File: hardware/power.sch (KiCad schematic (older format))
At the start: 34 parts, among them Q1 2n7002w, Q2 mmbt3906wt1, Q3 si2327ds, U1 TPS54526_PWP, U2 LT1761_1, U3 MIC2774N

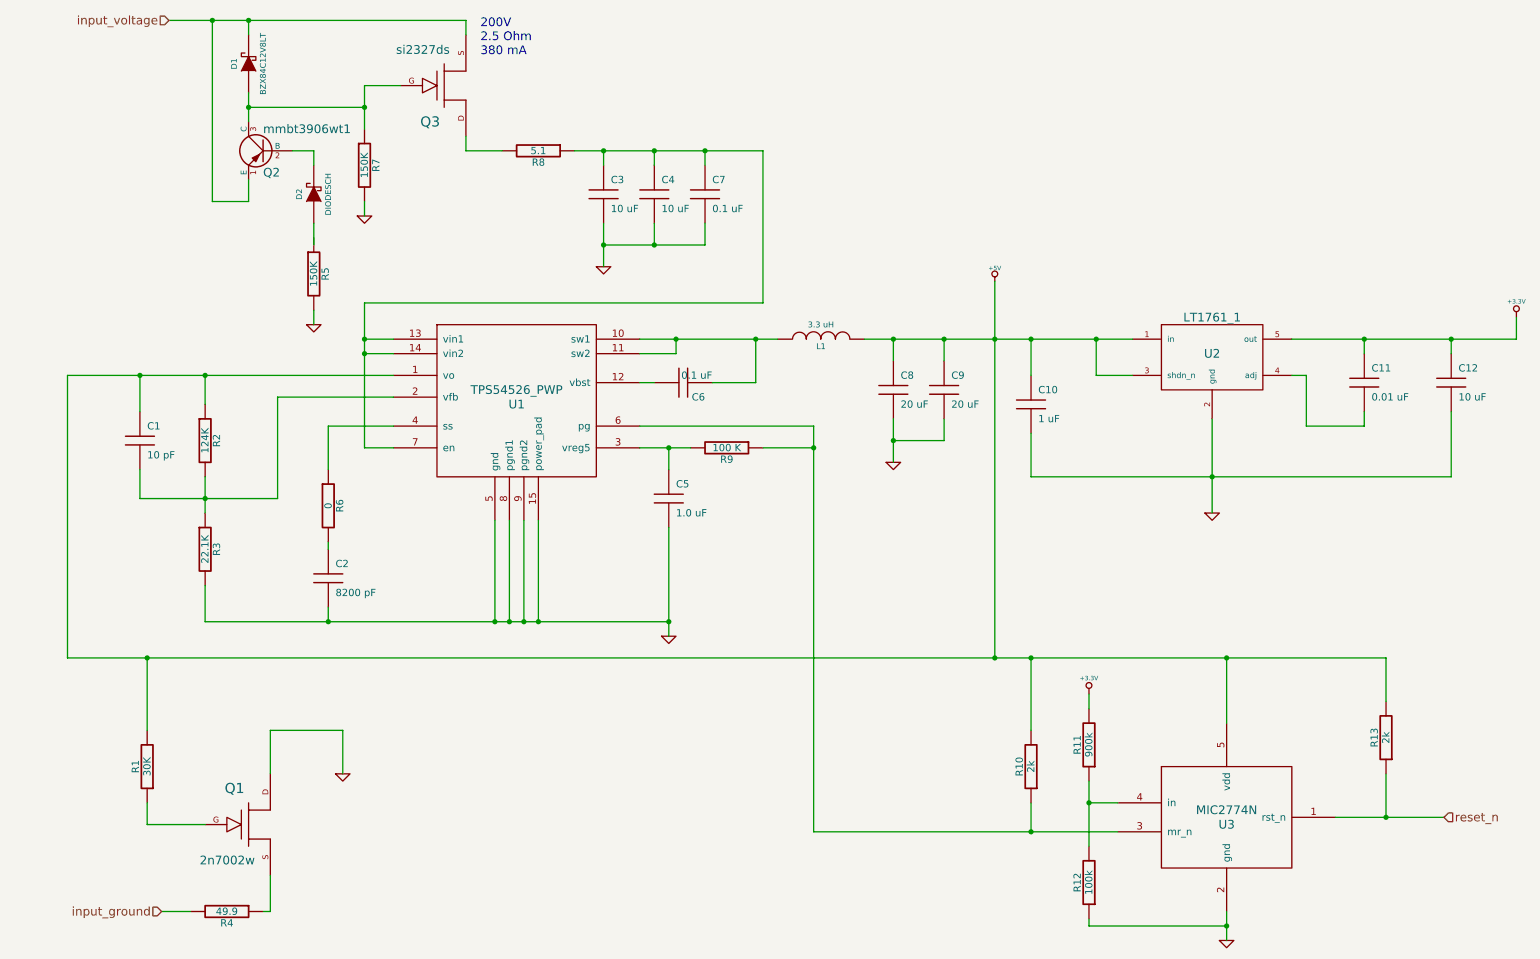
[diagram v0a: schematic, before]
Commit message: removed some protection
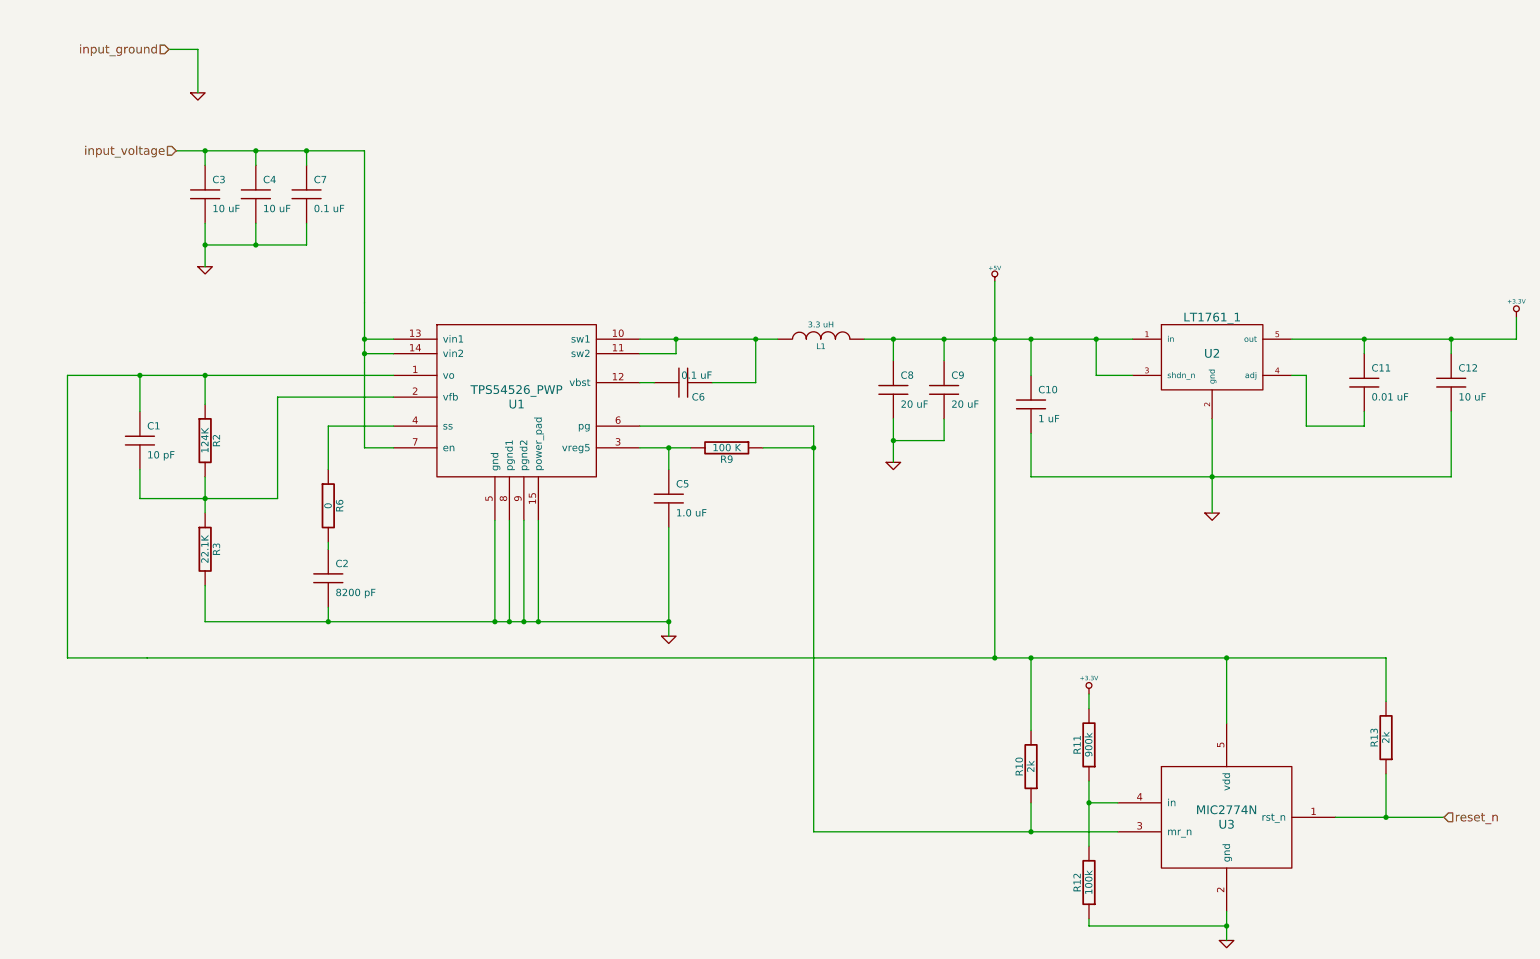
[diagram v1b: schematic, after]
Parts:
- removed D1: BZX84C12V8LT, symbol DIODESCH
- removed D2: DIODESCH, symbol DIODESCH
- removed Q1: 2n7002w, symbol FET_N
- removed Q2: mmbt3906wt1, symbol PNP
- removed Q3: si2327ds, symbol FET_N
- removed R1: 30K, symbol R
- removed R4: 49.9, symbol R
- removed R5, R7: 150K, symbol R
- removed R8: 5.1, symbol R
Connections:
- net input_voltage: now also C3.1, C4.1, C7.1, U1.13 (vin1), U1.14 (vin2), U1.7 (en)
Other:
- note removed: "200V \n2.5 Ohm \n380 mA"
- moved on the sheet: C3, C4, C7

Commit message: updated schematics to include new library and added uSD drive to processor
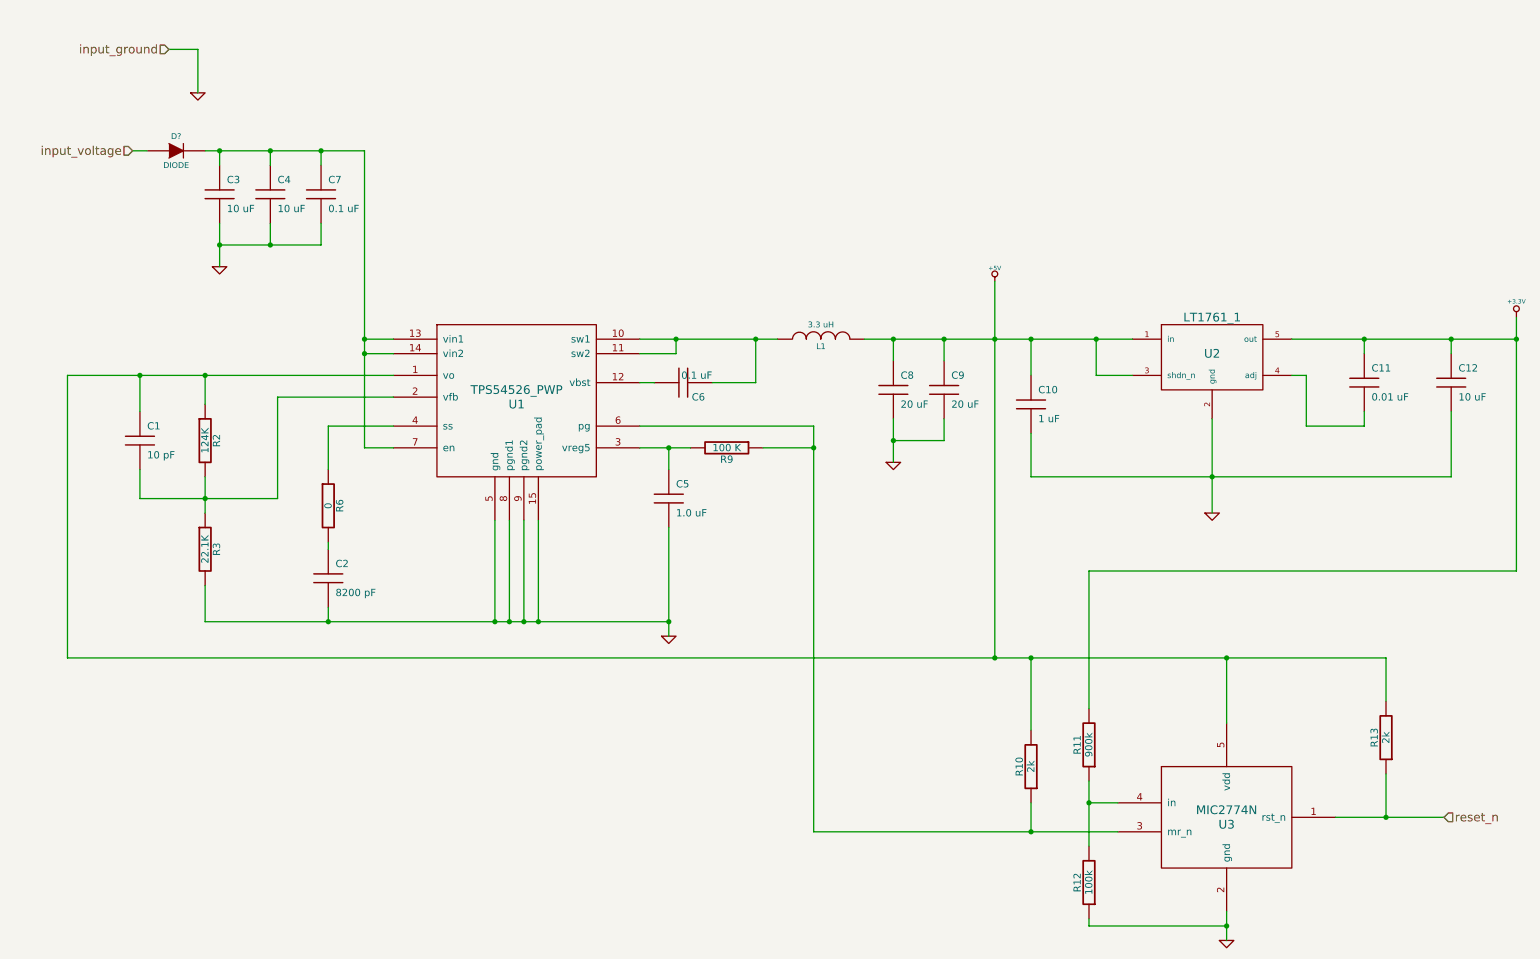
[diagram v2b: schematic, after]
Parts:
- added D?: DIODE, symbol DIODE
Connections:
- net input_voltage: now also D?.1 (A); no longer C3.1, C4.1, C7.1, U1.13 (vin1), U1.14 (vin2), U1.7 (en)
- new net: C3.1, C4.1, C7.1, D?.2 (K), U1.13 (vin1), U1.14 (vin2), U1.7 (en)
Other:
- moved on the sheet: C3, C4, C7
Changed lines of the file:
@@
-EESchema Schematic File Version 2  date Tue 04 Mar 2014 01:13:50 PM EST
+EESchema Schematic File Version 2  date Sat 26 Apr 2014 10:24:32 PM EDT
 LIBS:power
 LIBS:device
@@
 LIBS:valves
 LIBS:gs
+LIBS:opendous
 LIBS:eng_mon-cache
 EELAYER 25  0
@@
 Sheet 3 6
 Title ""
-Date "4 mar 2014"
+Date "27 apr 2014"
 Rev ""
 Comp ""
@@
 Comment4 ""
 $EndDescr
-Wire Wire Line
-	850  5100 1400 5100
-Wire Wire Line
-	1400 5100 7250 5100
+Connection ~ 10850 2900
+Wire Wire Line
+	10850 2750 10850 4500
+Wire Wire Line
+	10850 4500 7900 4500
+Wire Wire Line
+	7900 4500 7900 5450
+Wire Wire Line
+	1300 1600 1400 1600
 Connection ~ 5000 4850
 Wire Wire Line
-	5000 4950 5000 4850
-Wire Wire Line
-	5000 4850 5000 4200
-Wire Wire Line
-	2900 2650 2900 1600
-Wire Wire Line
-	2900 2650 2900 2650
-Wire Wire Line
-	2900 2650 2900 2900
-Wire Wire Line
-	2900 2900 2900 3000
-Wire Wire Line
-	2900 3000 2900 3650
+	5000 4200 5000 4950
+Wire Wire Line
+	2900 3650 2900 1600
 Wire Wire Line
 	1550 900  1750 900
 Wire Wire Line
-	7250 5100 7250 2900
-Wire Wire Line
-	7250 2900 7250 2500
-Wire Wire Line
-	8200 2900 7950 2900
-Wire Wire Line
-	7950 2900 7500 2900
-Wire Wire Line
-	7500 2900 7250 2900
-Wire Wire Line
-	7250 2900 6900 2900
-Wire Wire Line
-	6900 2900 6550 2900
-Wire Wire Line
-	6550 2900 6350 2900
+	7250 2500 7250 5100
+Wire Wire Line
+	6350 2900 8200 2900
 Connection ~ 6000 3650
 Connection ~ 7500 6300
 Wire Wire Line
-	8100 6300 7500 6300
-Wire Wire Line
-	7500 6300 6000 6300
-Wire Wire Line
-	6000 6300 6000 3650
-Wire Wire Line
-	6000 3650 6000 3500
+	8100 6300 6000 6300
+Wire Wire Line
+	6000 6300 6000 3500
 Connection ~ 4100 4850
 Wire Wire Line
-	5150 3650 5000 3650
-Wire Wire Line
-	5000 3650 4800 3650
+	4800 3650 5150 3650
 Connection ~ 1350 3150
 Wire Wire Line
@@
 	4800 3200 4900 3200
 Wire Wire Line
-	4800 2900 5050 2900
-Wire Wire Line
-	5050 2900 5600 2900
-Wire Wire Line
-	5600 2900 5750 2900
+	5750 2900 4800 2900
 Connection ~ 3900 4850
 Wire Wire Line
@@
 Wire Wire Line
 	3800 4850 3800 4150
-Connection ~ 1800 2250
-Wire Wire Line
-	1800 2250 2150 2250
-Wire Wire Line
-	2150 2250 2500 2250
-Wire Wire Line
-	2500 2250 2500 2100
-Connection ~ 2500 1600
-Wire Wire Line
-	2500 1700 2500 1600
-Wire Wire Line
-	1800 1600 1800 1700
+Connection ~ 1900 2250
+Wire Wire Line
+	1900 2250 2600 2250
+Wire Wire Line
+	2600 2250 2600 2100
+Connection ~ 2600 1600
+Wire Wire Line
+	2600 1600 2600 1700
+Wire Wire Line
+	1900 1600 1900 1700
 Wire Wire Line
 	3100 3000 2900 3000
@@
 	7900 6950 7900 6900
 Wire Wire Line
-	7900 5350 7900 5450
-Wire Wire Line
 	7500 6100 7500 6300
 Wire Wire Line
@@
 	9950 5400 9950 5100
 Wire Wire Line
-	9600 6200 9950 6200
-Wire Wire Line
-	9950 6200 10350 6200
+	10350 6200 9600 6200
 Wire Wire Line
 	10400 3400 10400 3850
 Wire Wire Line
-	10400 3850 8750 3850
-Wire Wire Line
-	8750 3850 7500 3850
-Wire Wire Line
-	9300 2900 9800 2900
-Wire Wire Line
-	9800 2900 10400 2900
-Wire Wire Line
-	10400 2900 10850 2900
+	10400 3850 7500 3850
+Wire Wire Line
+	10850 2900 9300 2900
 Connection ~ 9800 2900
 Wire Wire Line
@@
 	7950 3150 8200 3150
 Wire Wire Line
-	8750 4100 8750 3850
-Wire Wire Line
-	8750 3850 8750 3450
+	8750 3450 8750 4100
 Wire Wire Line
 	2650 4300 2650 4350
@@
 Connection ~ 8750 3850
 Wire Wire Line
-	10850 2900 10850 2750
-Wire Wire Line
 	9300 3150 9400 3150
 Wire Wire Line
@@
 Connection ~ 9950 6200
 Wire Wire Line
-	8850 6850 8850 6950
-Wire Wire Line
-	8850 6950 8850 7050
+	8850 7050 8850 6850
 Wire Wire Line
 	7500 5100 7500 5600
 Connection ~ 8850 5100
 Wire Wire Line
-	7900 6400 7900 6100
-Wire Wire Line
-	7900 6100 7900 5950
+	7900 5950 7900 6400
 Connection ~ 7900 6100
 Wire Wire Line
@@
 Connection ~ 2900 2900
 Wire Wire Line
-	2150 1600 2150 1700
-Connection ~ 2150 1600
-Wire Wire Line
-	1800 2100 1800 2250
-Wire Wire Line
-	1800 2250 1800 2400
-Wire Wire Line
-	2150 2100 2150 2250
-Connection ~ 2150 2250
+	2250 1600 2250 1700
+Connection ~ 2250 1600
+Wire Wire Line
+	1900 2400 1900 2100
+Wire Wire Line
+	2250 2100 2250 2250
+Connection ~ 2250 2250
 Wire Wire Line
 	4100 4150 4100 4850
@@
 Connection ~ 5600 2900
 Wire Wire Line
-	6550 3750 6550 3600
-Wire Wire Line
-	6550 3600 6550 3450
+	6550 3450 6550 3750
 Connection ~ 6550 3600
 Wire Wire Line
-	6550 2900 6550 3050
+	6550 3050 6550 2900
 Connection ~ 6550 2900
 Wire Wire Line
@@
 	850  3150 850  5100
 Wire Wire Line
-	850  3150 1350 3150
-Wire Wire Line
-	1350 3150 1800 3150
-Wire Wire Line
-	1800 3150 3100 3150
-Wire Wire Line
-	1800 4850 2650 4850
-Wire Wire Line
-	2650 4850 3800 4850
-Wire Wire Line
-	3800 4850 3900 4850
-Wire Wire Line
-	3900 4850 4000 4850
-Wire Wire Line
-	4000 4850 4100 4850
-Wire Wire Line
-	4100 4850 5000 4850
+	850  3150 3100 3150
+Wire Wire Line
+	1800 4850 5000 4850
 Connection ~ 2650 4850
 Wire Wire Line
-	1800 3850 1800 4000
-Wire Wire Line
-	1800 4000 1800 4100
+	1800 4100 1800 3850
 Wire Wire Line
 	3100 3300 2300 3300
@@
 	1350 3800 1350 4000
 Wire Wire Line
-	1350 4000 1800 4000
-Wire Wire Line
-	1800 4000 2300 4000
+	1350 4000 2300 4000
 Wire Wire Line
 	5000 3800 5000 3650
@@
 Connection ~ 7250 2900
 Wire Wire Line
-	7250 5100 7500 5100
-Wire Wire Line
-	7500 5100 8850 5100
-Wire Wire Line
-	8850 5100 9950 5100
+	850  5100 9950 5100
 Connection ~ 7500 5100
 Connection ~ 7250 5100
 Wire Wire Line
 	1750 900  1750 1200
-Wire Wire Line
-	2900 1600 2500 1600
-Wire Wire Line
-	2500 1600 2150 1600
-Wire Wire Line
-	2150 1600 1800 1600
-Wire Wire Line
-	1800 1600 1600 1600
-Connection ~ 1800 1600
+Connection ~ 1900 1600
+Wire Wire Line
+	2900 1600 1800 1600
+$Comp
+L DIODE D?
+U 1 1 534ECE6D
+P 1600 1600
+F 0 "D?" H 1600 1700 40  0000 C CNN
+F 1 "DIODE" H 1600 1500 40  0000 C CNN
+	1    1600 1600
+	1    0    0    -1
+$EndComp
 $Comp
 L GND #PWR03
@@
 L GND #PWR06
 U 1 1 52784FA3
-P 1800 2400
-F 0 "#PWR06" H 1800 2400 30  0001 C CNN
-F 1 "GND" H 1800 2330 30  0001 C CNN
-	1    1800 2400
+P 1900 2400
+F 0 "#PWR06" H 1900 2400 30  0001 C CNN
+F 1 "GND" H 1900 2330 30  0001 C CNN
+	1    1900 2400
 	1    0    0    -1
 $EndComp
@@
 L C C7
 U 1 1 52784F6E
-P 2500 1900
-F 0 "C7" H 2550 2000 50  0000 L CNN
-F 1 "0.1 uF" H 2550 1800 50  0000 L CNN
-	1    2500 1900
+P 2600 1900
+F 0 "C7" H 2650 2000 50  0000 L CNN
+F 1 "0.1 uF" H 2650 1800 50  0000 L CNN
+	1    2600 1900
 	1    0    0    -1
 $EndComp
@@
 L C C4
 U 1 1 52784F63
-P 2150 1900
-F 0 "C4" H 2200 2000 50  0000 L CNN
-F 1 "10 uF" H 2200 1800 50  0000 L CNN
-	1    2150 1900
+P 2250 1900
+F 0 "C4" H 2300 2000 50  0000 L CNN
+F 1 "10 uF" H 2300 1800 50  0000 L CNN
+	1    2250 1900
 	1    0    0    -1
 $EndComp
@@
 L C C3
 U 1 1 52784F2D
-P 1800 1900
-F 0 "C3" H 1850 2000 50  0000 L CNN
-F 1 "10 uF" H 1850 1800 50  0000 L CNN
-	1    1800 1900
+P 1900 1900
+F 0 "C3" H 1950 2000 50  0000 L CNN
+F 1 "10 uF" H 1950 1800 50  0000 L CNN
+	1    1900 1900
 	1    0    0    -1
 $EndComp
@@
 F 1 "0" V 2650 4050 50  0000 C CNN
 	1    2650 4050
-	1    0    0    -1
-$EndComp
-$Comp
-L +3.3V #PWR07
-U 1 1 526E4845
-P 7900 5350
-F 0 "#PWR07" H 7900 5310 30  0001 C CNN
-F 1 "+3.3V" H 7900 5460 30  0000 C CNN
-	1    7900 5350
 	1    0    0    -1
 $EndComp
@@
 Text HLabel 1550 900  0    60   Input ~ 0
 input_ground
-Text HLabel 1600 1600 0    60   Input ~ 0
+Text HLabel 1300 1600 0    60   Input ~ 0
 input_voltage
 $EndSCHEMATC

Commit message: fixed some ERCs and simplified reset
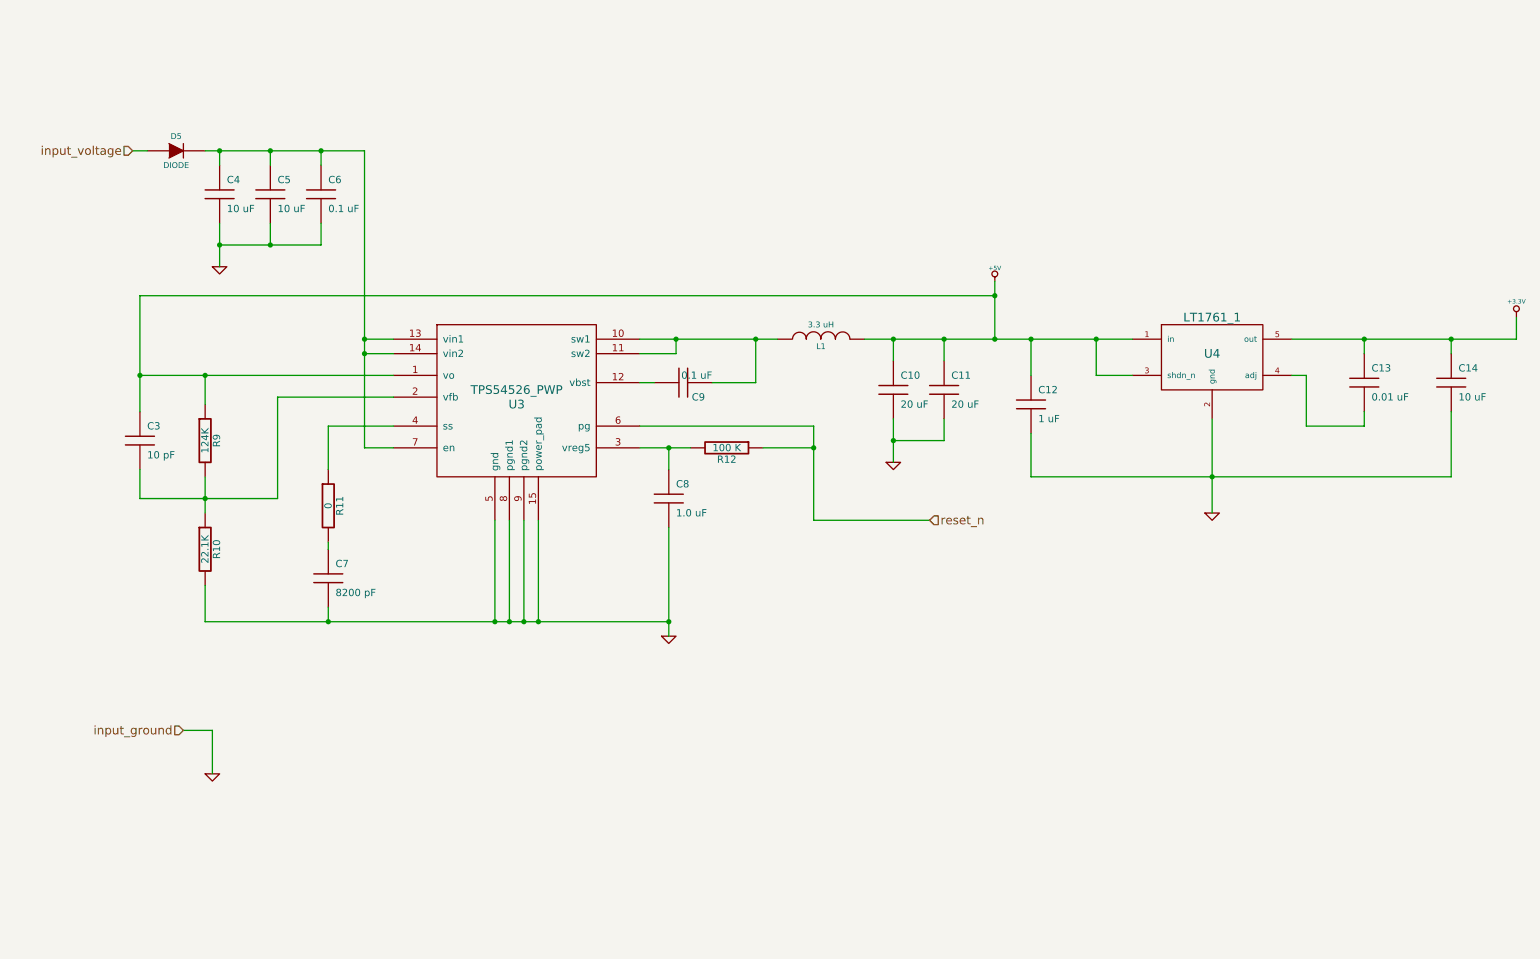
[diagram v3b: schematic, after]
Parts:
- removed R10, R13: 2k, symbol R
- removed R11: 900k, symbol R
- removed R12: 100k, symbol R
- removed U3: MIC2774N, symbol MIC2774N
- gave numbers to parts that had none: 1
- renumbered C8 to C10, C9 to C11, C10 to C12, C11 to C13, C12 to C14, C1 to C3, C3 to C4, C4 to C5, C7 to C6, C2 to C7, C5 to C8, C6 to C9, R3 to R10, R6 to R11, R9 to R12, R2 to R9, U1 to U3, U2 to U4
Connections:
- net reset_n: now also R12.1, U3.6 (pg)
